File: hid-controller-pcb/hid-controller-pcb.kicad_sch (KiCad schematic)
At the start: 11 parts, among them J1 10118194-0011LF, SW1 SW_Push, U1 STM32F103C8Tx, Y1 8MHz

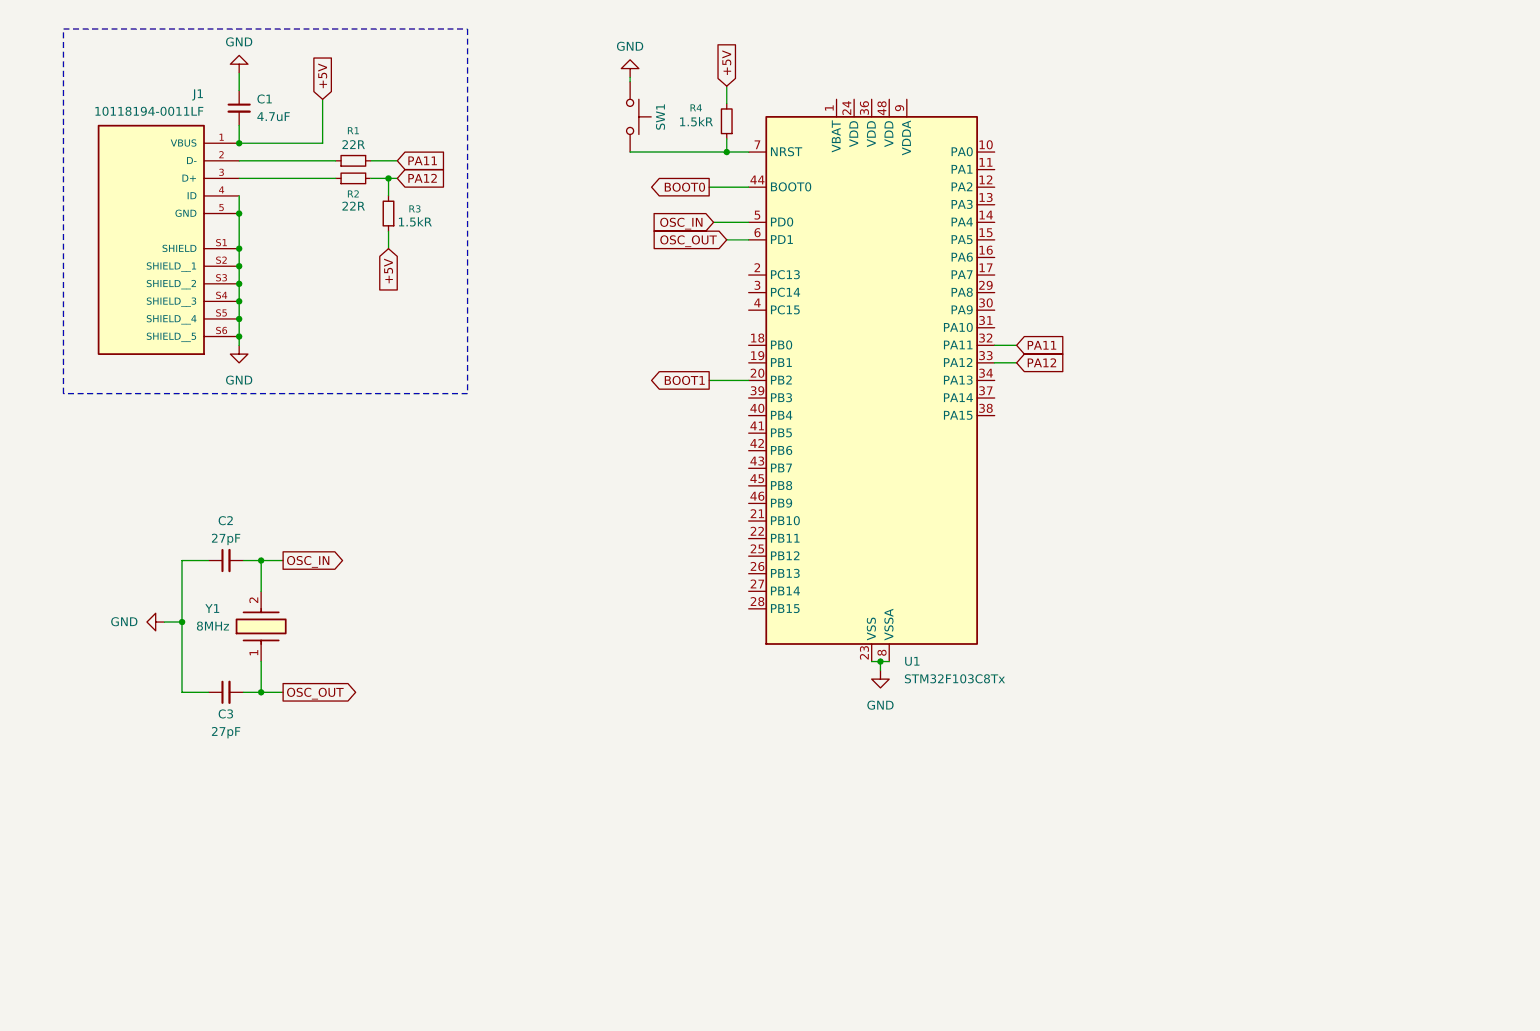
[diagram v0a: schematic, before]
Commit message: HSE / LSE finished, onto analog
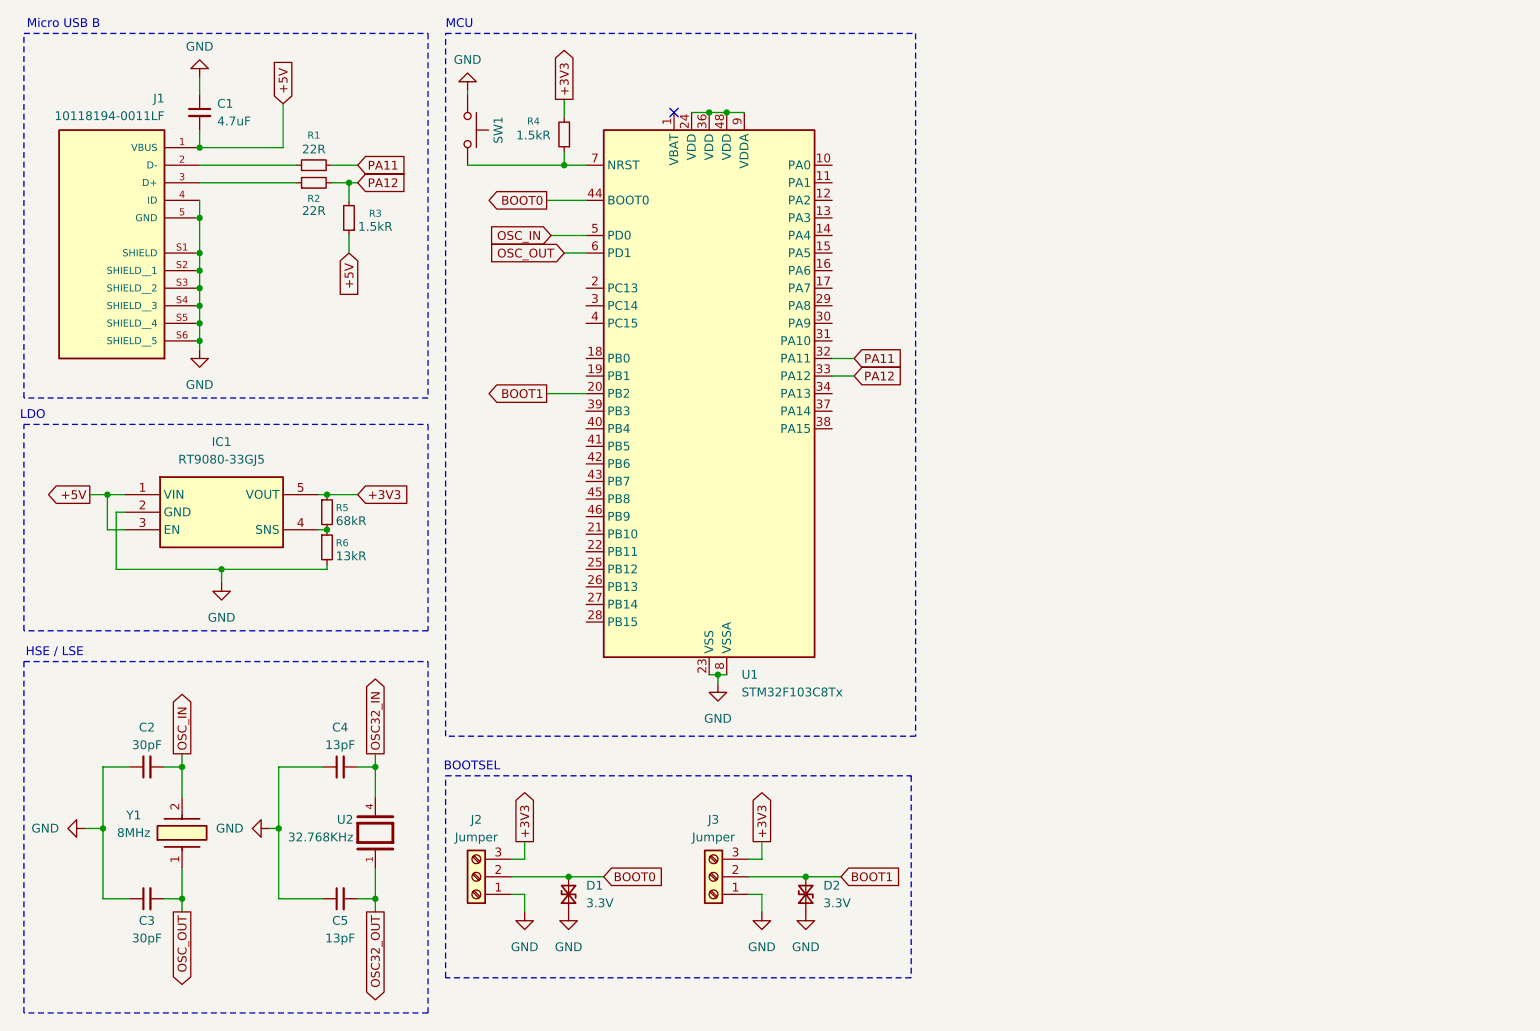
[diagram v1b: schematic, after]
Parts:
- added C4, C5: 13pF, symbol Device:C_Small
- added D1, D2: 3.3V, symbol Device:D_TVS_Small
- added IC1: RT9080-33GJ5, lib:RT9080-33GJ5, symbol library:RT9080-33GJ5
- added J2, J3: Jumper, symbol Connector:Screw_Terminal_01x03
- added R5: 68kR, symbol Device:R_Small
- added R6: 13kR, symbol Device:R_Small
- added U2: 32.768KHz, lib:CM200C32768DZCT, symbol library:CM200C32768DZCT
- C2, C3: value 27pF -> 30pF
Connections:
- net +5V: now also IC1.1 (VIN), IC1.3 (EN); no longer R4.2
- net BOOT0: now also D1.2 (A2), J2.2 (Pin_2)
- net BOOT1: now also D2.2 (A2), J3.2 (Pin_2)
- net GND: now also C4.1, C5.1, D1.1 (A1), D2.1 (A1), IC1.2 (GND), J2.1 (Pin_1), J3.1 (Pin_1), R6.2
- net at U1.24 (VDD): now also U1.36 (VDD), U1.48 (VDD), U1.9 (VDDA)
- new net: IC1.4 (SNS), R5.2, R6.1
- new net +3V3: IC1.5 (VOUT), J2.3 (Pin_3), J3.3 (Pin_3), R4.2, R5.1
- new net OSC32_IN: C4.2, U2.4
- new net OSC32_OUT: C5.2, U2.1
- no-connect marks 0 -> 1
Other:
- note added: "BOOTSEL"
- note added: "HSE / LSE"
- note added: "LDO"
- note added: "MCU"
- note added: "Micro USB B"
- moved on the sheet: C1, C2, C3, J1, R1, R2, R3, R4, SW1, U1, Y1

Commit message: .
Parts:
- removed D2: 3.3V, symbol Device:D_TVS_Small
- removed J3: Jumper, symbol Connector:Screw_Terminal_01x03
- added R7, R8: 1.5kR, symbol Device:R_Small
- added U3, U4: COM-09032, lib:XDCR_COM-09032, symbol library:COM-09032
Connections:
- net BOOT1 is gone; now on net GND: U1.20 (PB2)
- net +3V3: now also R7.1, R8.1, U3.H1 (H+), U3.V1 (V+), U4.H1 (H+), U4.V1 (V+)
- net GND: now also U3.B2A (SEL-), U3.H3 (H-), U3.S1 (SHIELD), U3.S2 (SHIELD), U3.S3 (SHIELD), U3.S4 (SHIELD), U3.V3 (V-), U4.B2A (SEL-), U4.H3 (H-), U4.S1 (SHIELD), U4.S2 (SHIELD), U4.S3 (SHIELD), U4.S4 (SHIELD), U4.V3 (V-)
- net OSC32_IN: now also U1.3 (PC14)
- net OSC32_OUT: now also U1.4 (PC15)
- net AN_A1: now reaches U1.11 (PA1)
- net AN_A1: now also U3.V2 (V)
- net AN_B1: now reaches U1.12 (PA2)
- net AN_B1: now also U3.H2 (H)
- net AN_A2: now reaches U1.14 (PA4)
- net AN_A2: now also U4.V2 (V)
- net AN_B2: now reaches U1.15 (PA5)
- net AN_B2: now also U4.H2 (H)
- net AN_SEL1: now reaches U1.21 (PB10)
- net AN_SEL1: now also R7.2, U3.B1A (SEL+)
- net AN_SEL2: now reaches U1.22 (PB11)
- net AN_SEL2: now also R8.2, U4.B1A (SEL+)
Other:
- note added: "JOYSTICKS"
- note added: "LEFT"
- note added: "RIGHT"
- moved on the sheet: D1, J2
